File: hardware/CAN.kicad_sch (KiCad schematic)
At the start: 5 parts, among them U6 MCP2562-H-SN

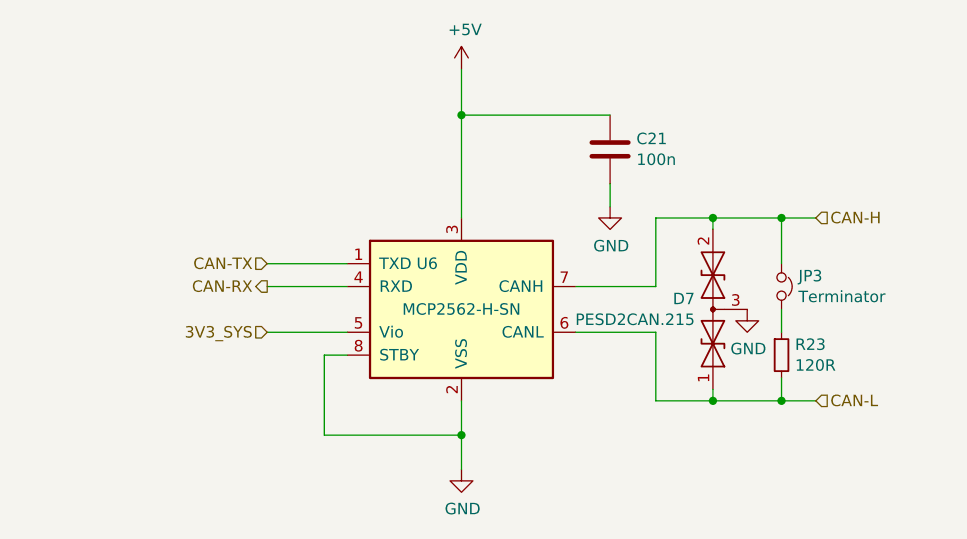
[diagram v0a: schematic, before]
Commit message: Add brake pressure sensors
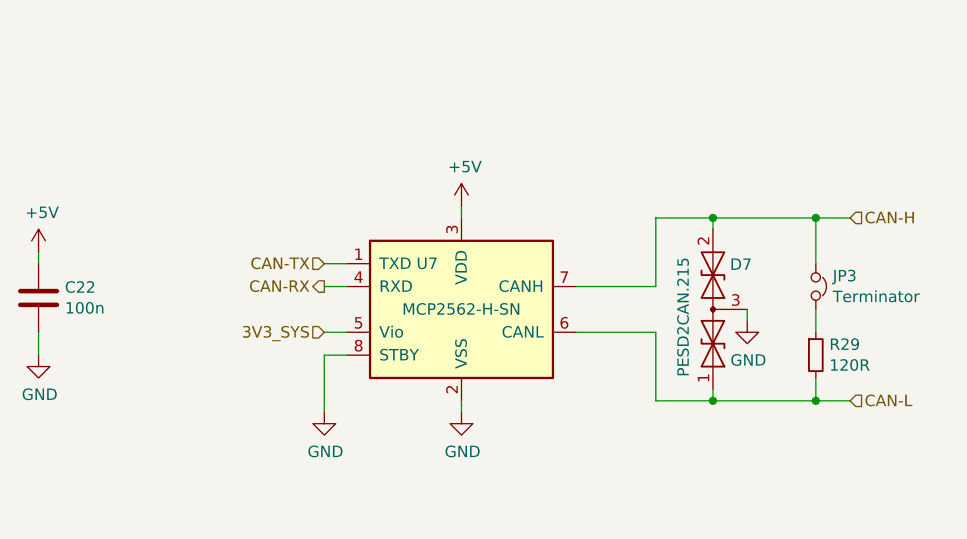
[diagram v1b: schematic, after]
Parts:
- renumbered C21 to C22, R23 to R29, U6 to U7
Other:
- moved on the sheet: C22, JP3, R29
